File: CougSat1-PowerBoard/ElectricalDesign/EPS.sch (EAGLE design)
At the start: 250 parts, among them J1 PV0, J2 PV1, J3 PV2, J4 PV3, J5 Umbilical, J6 SWD, J7 CougSat Card, J8 Deployables, Q1 NTLUD3A50PZ, Q10 DMN2008LFU, Q11 DMN2008LFU, Q12 CSD25402Q3A, Q13 CSD25402Q3A, Q14 NTLUD3A50PZ, Q15 NTLUD3A50PZ, Q16 NTLUD3A50PZ, Q17 NTLUD3A50PZ, Q18 NTLUD3A50PZ, Q19 NTLUD3A50PZ, Q2 NTLUD3A50PZ, Q20 NTLUD3A50PZ, Q21 NTLUD3A50PZ, Q22 NTLUD3A50PZ, Q23 CSD25402Q3A, Q24 CSD25402Q3A, Q25 DMN53D0L, Q26 NTLUD3A50PZ, Q27 NTLUD3A50PZ, Q28 NTLUD3A50PZ, Q29 NTLUD3A50PZ, Q3 NTLUD3A50PZ, Q30 NTLUD3A50PZ, Q31 NTLUD3A50PZ, Q32 NTLUD3A50PZ, Q33 NTLUD3A50PZ, Q34 NTLUD3A50PZ, Q35 NTLUD3A50PZ, Q36 NTLUD3A50PZ, Q37 NTLUD3A50PZ, Q38 NTLUD3A50PZ, Q39 NTLUD3A50PZ, Q4 NTLUD3A50PZ, Q40 NTLUD3A50PZ, Q41 NTLUD3A50PZ, Q42 NTLUD3A50PZ, Q43 NTLUD3A50PZ, Q5 NTLUD3A50PZ, Q6 NTLUD3A50PZ, Q7 NTLUD3A50PZ, Q8 NTLUD3A50PZ, Q9 NTLUD3A50PZ, SW1 D2MQ-1-TL, U1 BQ29700, U10 LTC2499, U11 LTC2499, U12 LTC2499, U13 LTC2499, U14 MCP1501-18, U15 LTC2499, U2 BQ29700, U3 TPS64200, U4 TPS64200, U5 STM32L476RGT, U6 TCA9535R, U7 SN74LVC244AR, U8 TCA9535R, U9 LTC2499

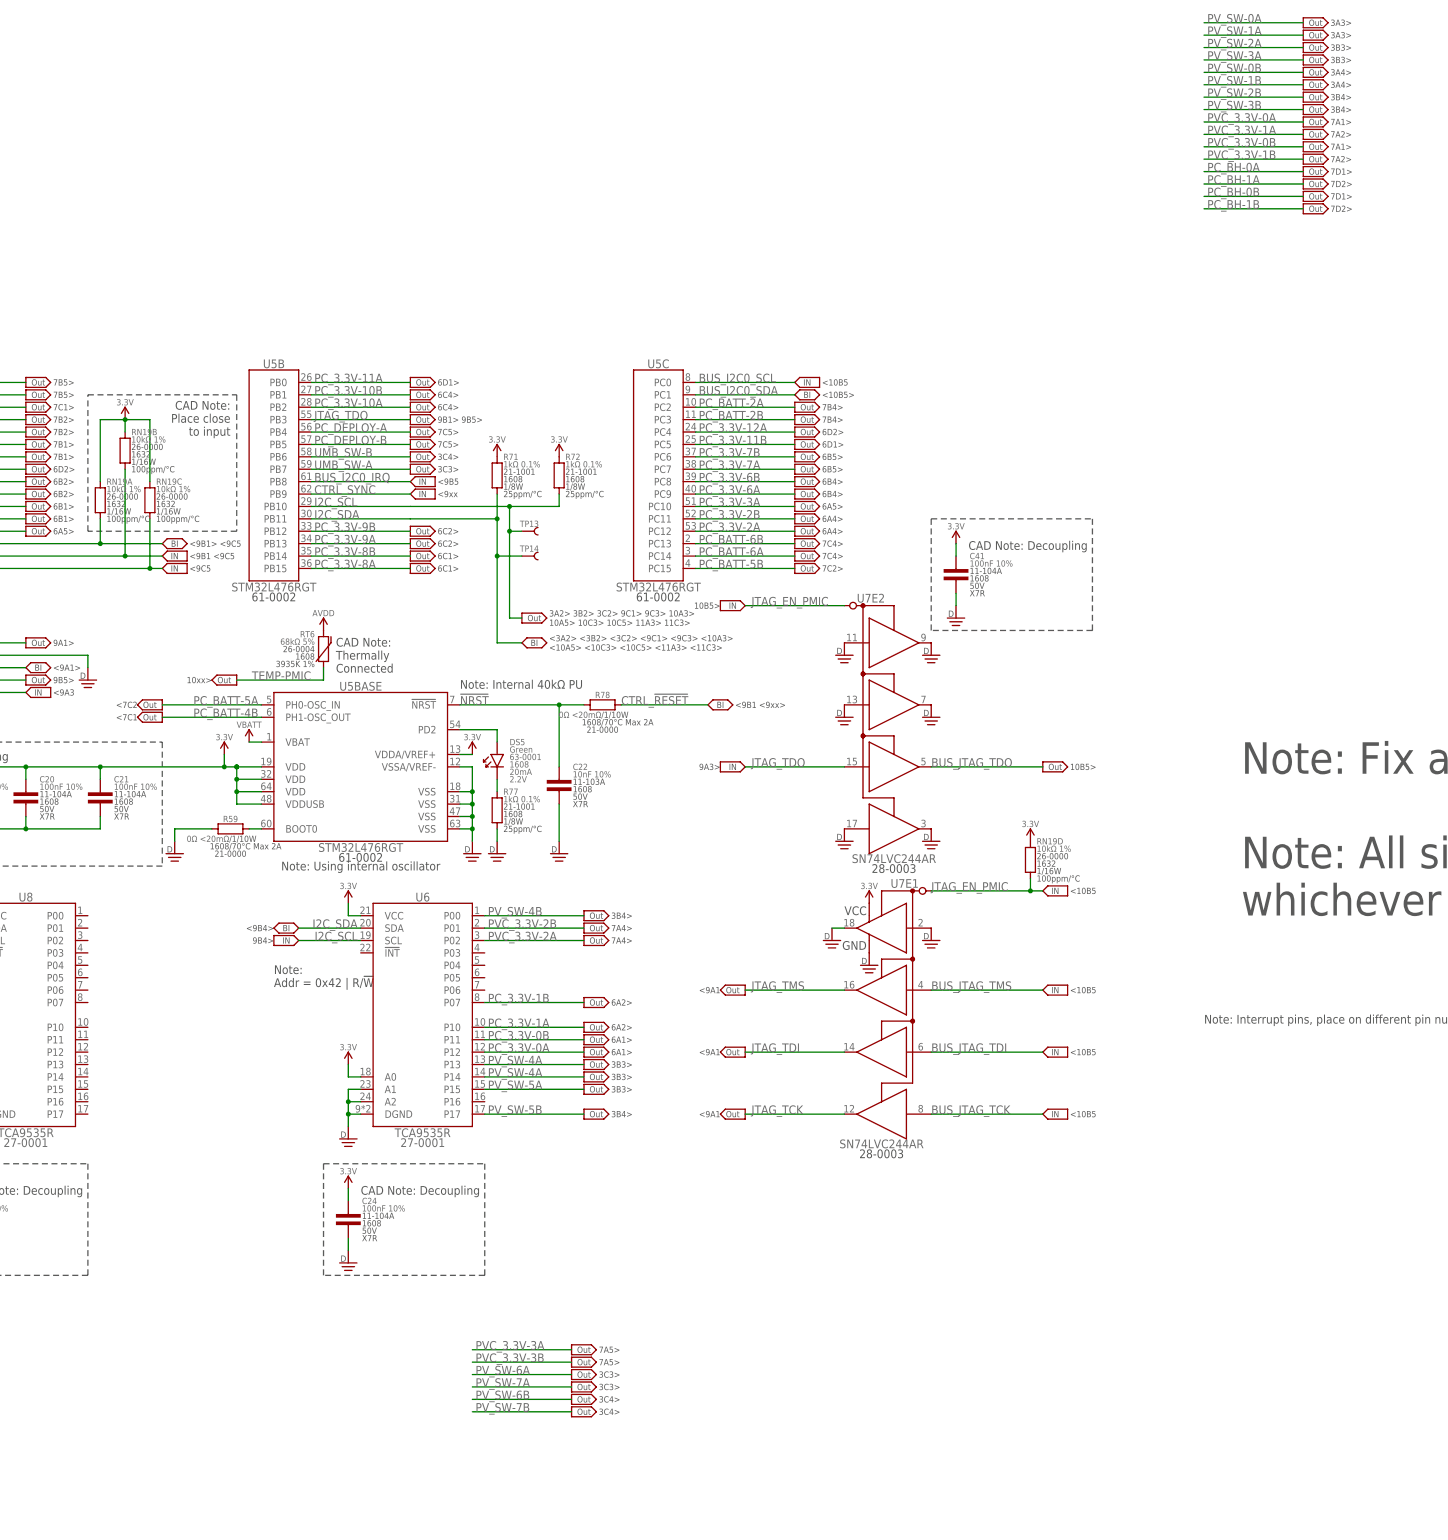
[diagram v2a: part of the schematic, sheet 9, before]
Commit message: Laid Out 3V3A Regulator
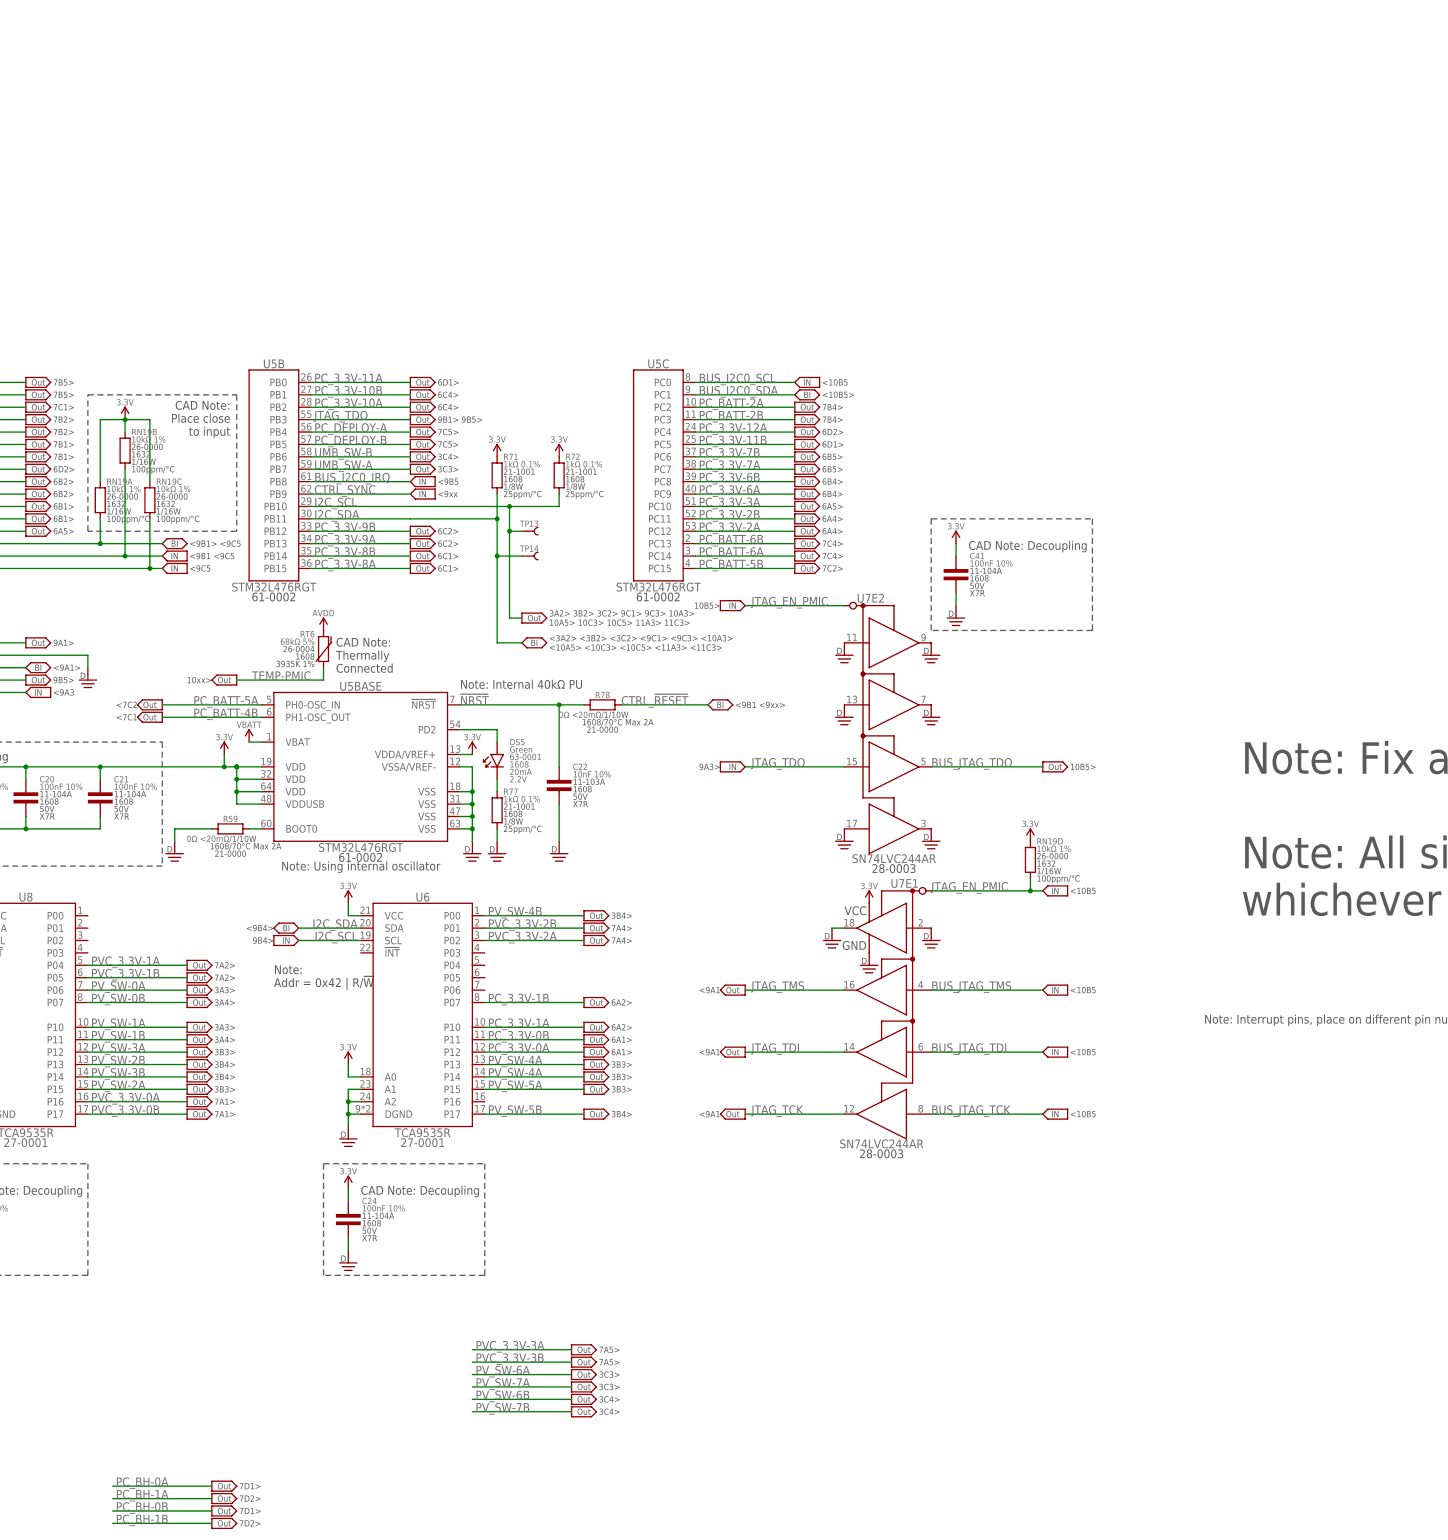
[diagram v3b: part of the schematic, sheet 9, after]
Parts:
- removed RN4, RN5: 10kΩ 5%, CougsInSpace-Resistors:RES_BUS-10-10K-3264
- added R86, R87, R88, R89: 10kΩ 0.1%, CougsInSpace-Resistors:RES-V-10K-1608
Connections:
- net 3.3V: now also R86.2, R87.2, R88.2, R89.2; no longer RN4.C, RN5.C
- net 3.3V-A: now also U12.CH6
- net 3.3V_I-A: now also U12.CH7
- net 3.3V_ISENS-A: now also U12.CH8
- net BP_VSS-A: now also U12.CH13
- net BP_VSS-B: now also U12.CH11
- net BP_VSS_I-A: now also U12.CH12
- net BP_VSS_I-B: now also U12.CH10
- net I_BH-0: now also U12.CH3
- net PR_BH-0: now also U12.CH2
- net PVC_3.3V-0A: now also R86.1, U8.P16
- net PVC_3.3V-0B: now also R87.1, U8.P17
- net PVC_3.3V-1A: now also R88.1, U8.P04
- net PVC_3.3V-1B: now also R89.1, U8.P05
- net PVI_3.3V-0: now also U12.CH1
- net PVI_3.3V-1: now also U12.CH15
- net PV_3.3V-0: now also U12.CH0
- net PV_3.3V-1: now also U12.CH14
- net PV_SW-0A: now also U8.P06
- net PV_SW-0B: now also RN20.8, U8.P07; no longer RN20.2
- net PV_SW-1A: now also RN20.2, U8.P10; no longer RN20.3
- net PV_SW-1B: now also RN20.7, U8.P11; no longer RN20.4
- net PV_SW-2A: now also U8.P15
- net PV_SW-2B: now also U8.P13
- net PV_SW-3A: now also RN20.3, U8.P12; no longer RN20.7
- net PV_SW-3B: now also RN20.4, U8.P14; no longer RN20.8
- net VBATT-A: now also U12.CH5, U12.CH9
- net VIN-A: now also U12.CH4

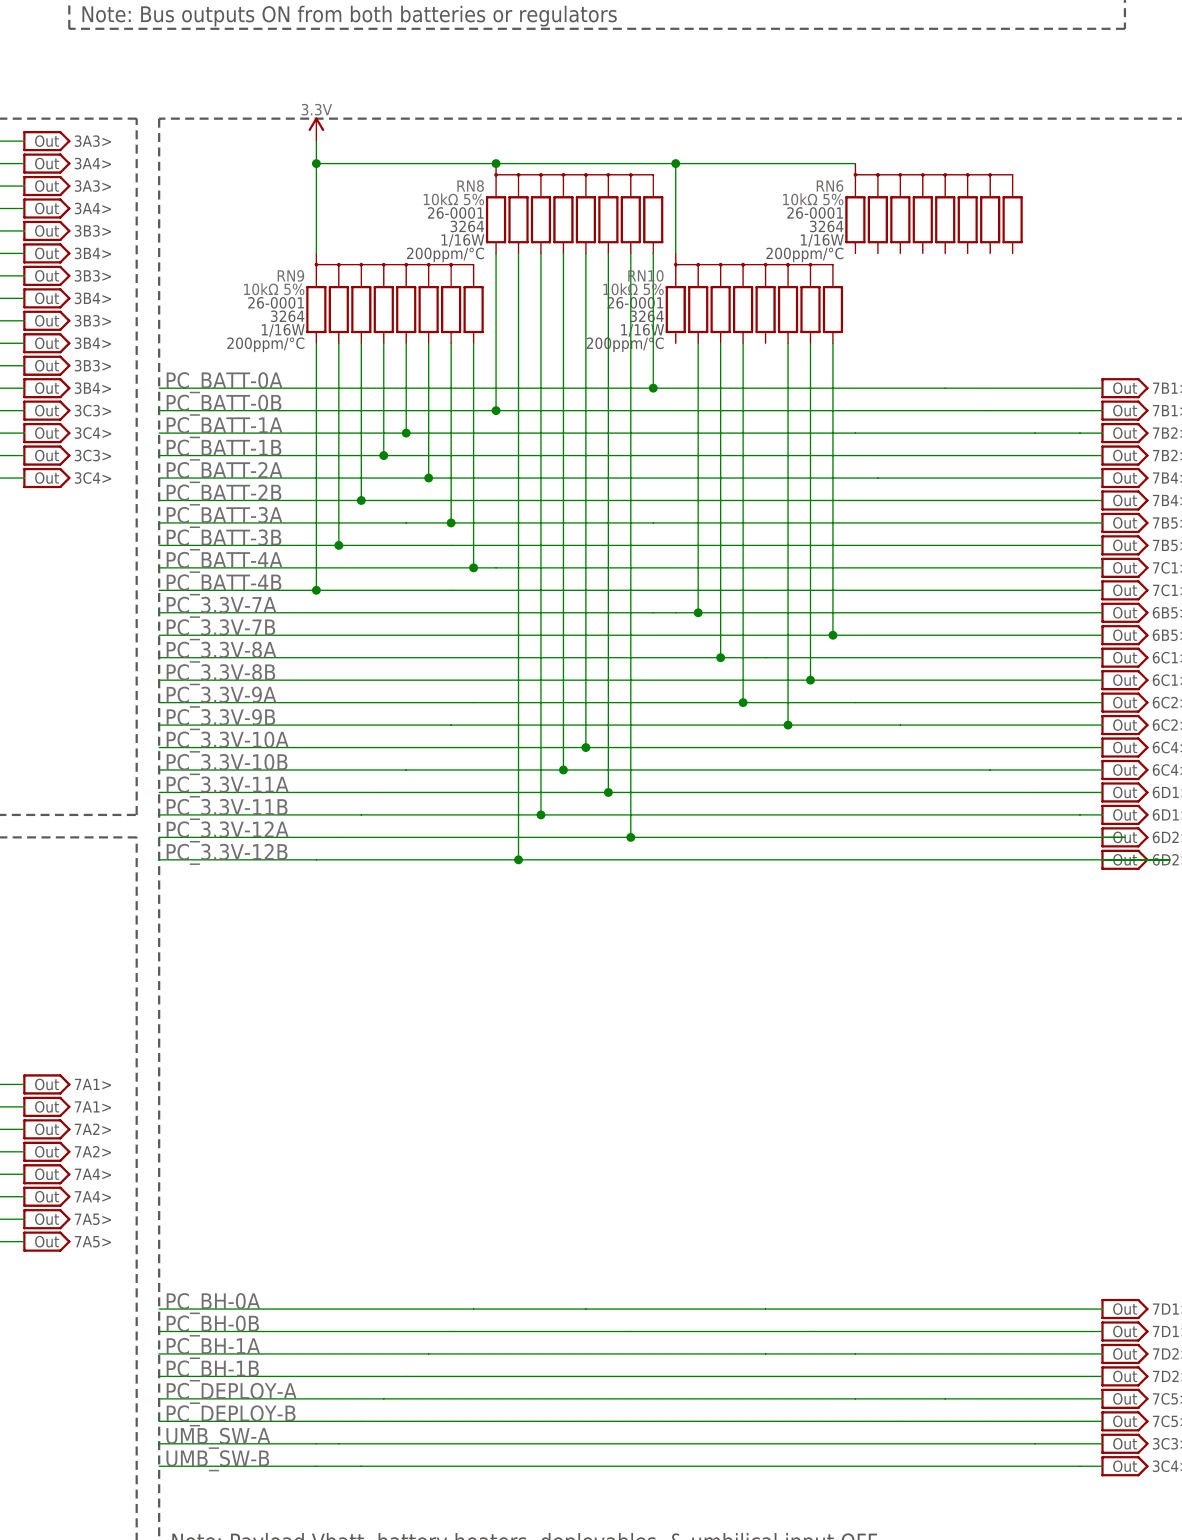
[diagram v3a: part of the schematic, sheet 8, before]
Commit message: Laid Out Voltage ADC
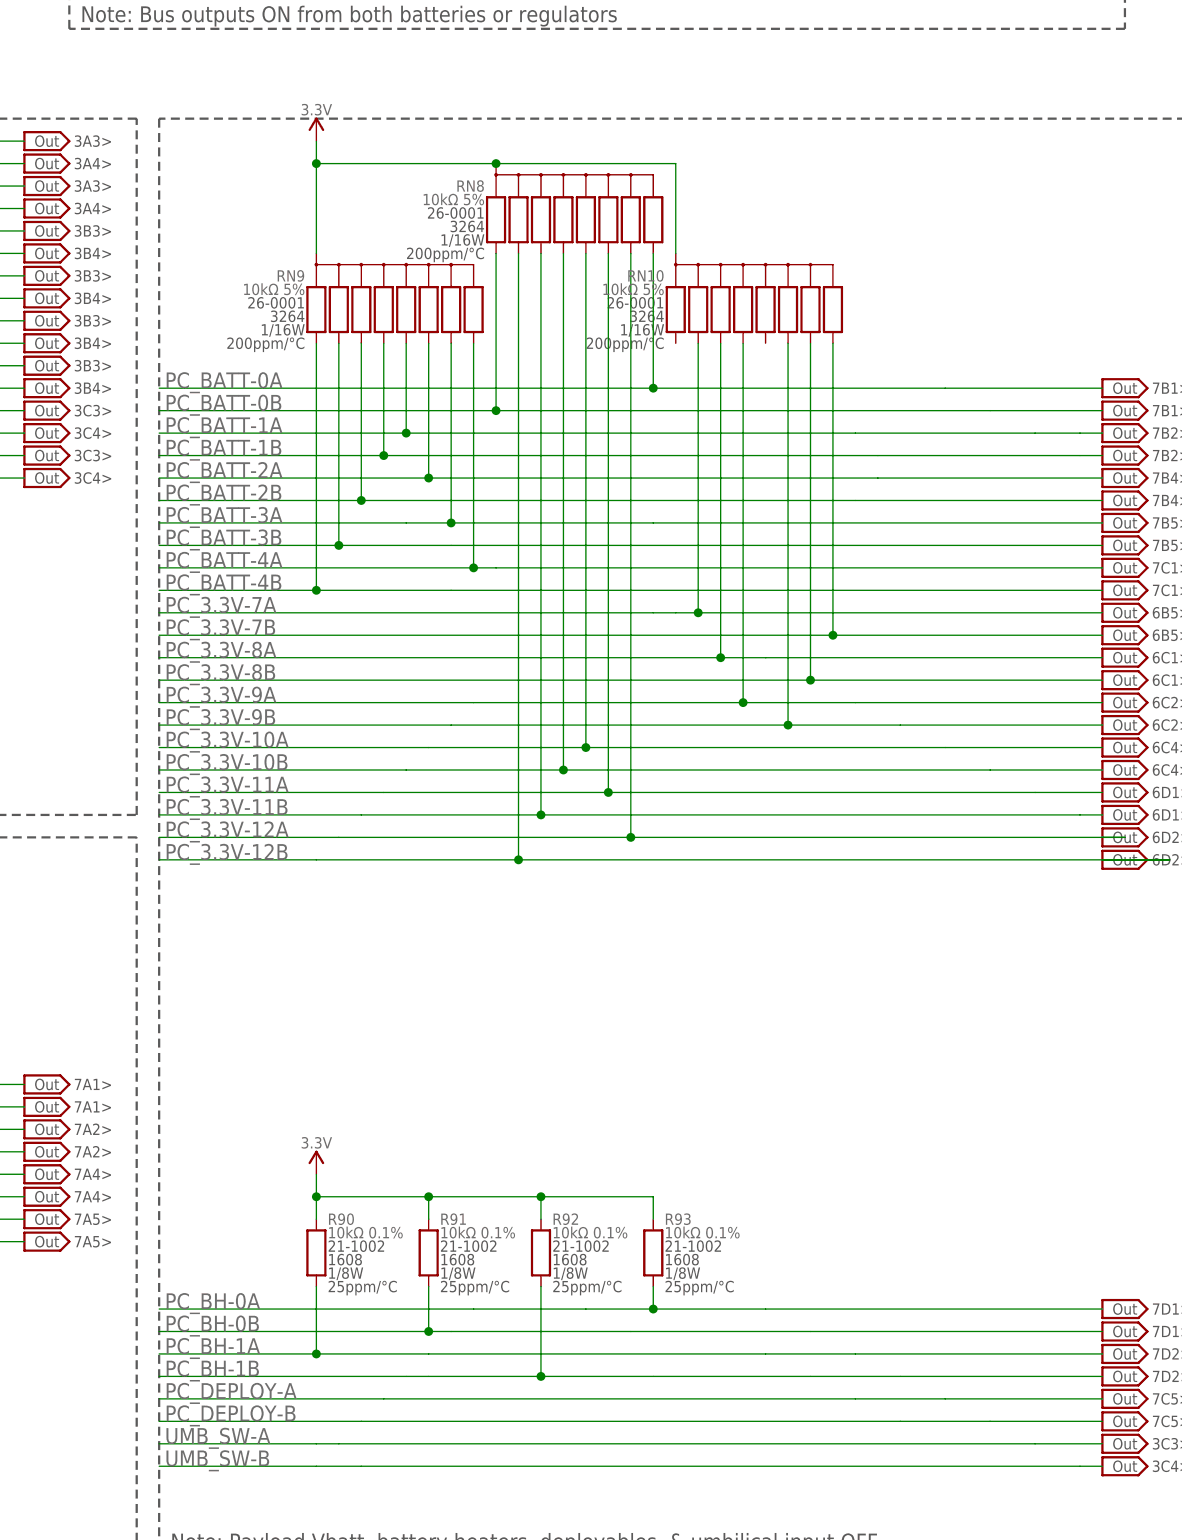
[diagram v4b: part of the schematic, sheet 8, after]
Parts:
- removed RN6: 10kΩ 5%, CougsInSpace-Resistors:RES_BUS-10-10K-3264
- added R90, R91, R92, R93: 10kΩ 0.1%, CougsInSpace-Resistors:RES-V-10K-1608
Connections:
- net 3.3V: now also R90.2, R91.2, R92.2, R93.2; no longer RN6.C
- net 3.3V-A: now also U13.CH11; no longer U13.CH13
- net 3.3V-B: now also U13.CH12; no longer U13.CH14
- net I_BH-0: now also U12.CH2; no longer U12.CH3
- net PC_BH-0A: now also R93.1, U8.P02
- net PC_BH-0B: now also R91.1, U8.P03
- net PC_BH-1A: now also R90.1, U8.P00
- net PC_BH-1B: now also R92.1, U8.P01
- net PR_BH-0: now also U12.CH3; no longer U12.CH2
- net TEMP+X+Y: now also U13.CH4; no longer U13.CH2
- net TEMP-BATT-B: now also U13.CH13; no longer U13.CH11
- net TEMP-PMIC: now also U13.CH2; no longer U13.CH4
- net TEMP-REG-B: now also U13.CH14; no longer U13.CH15
- net VBATT-B: now also U13.CH15; no longer U13.CH12

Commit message: Laid Out JTAG
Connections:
- net UMB_SW-A: now also U5B.PB6; no longer U5B.PB7
- net UMB_SW-B: now also U5B.PB7; no longer U5B.PB6
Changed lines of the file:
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@@
 <text x="154.94" y="-25.4" size="1.27" layer="97" align="center-left"> 3C4&gt;</text>
 <text x="76.2" y="58.42" size="1.27" layer="97" align="center-left"> 3A4&gt;</text>
-<text x="121.92" y="167.64" size="1.27" layer="97" align="center-left"> 3C3&gt;</text>
-<text x="121.92" y="170.18" size="1.27" layer="97" align="center-left"> 3C4&gt;</text>
+<text x="121.92" y="170.18" size="1.27" layer="97" align="center-left"> 3C3&gt;</text>
+<text x="121.92" y="167.64" size="1.27" layer="97" align="center-left"> 3C4&gt;</text>
 <text x="287.02" y="93.98" size="6.4516" layer="97" align="center-left">Note: Fix all off sheet designators linked to this sheet (JTAG too)
 Note: All signals above are GPIO, connect to any GPIO bank,
@@
 <net name="UMB_SW-A" class="0">
 <segment>
-<wire x1="96.52" y1="167.64" x2="116.84" y2="167.64" width="0.1524" layer="91"/>
-<label x="97.155" y="167.64" size="1.778" layer="95"/>
-<pinref part="U5" gate="B" pin="PB7"/>
-</segment>
-</net>
-<net name="UMB_SW-B" class="0">
-<segment>
 <wire x1="96.52" y1="170.18" x2="116.84" y2="170.18" width="0.1524" layer="91"/>
 <label x="97.155" y="170.18" size="1.778" layer="95"/>
@@
 </segment>
 </net>
+<net name="UMB_SW-B" class="0">
+<segment>
+<wire x1="96.52" y1="167.64" x2="116.84" y2="167.64" width="0.1524" layer="91"/>
+<label x="97.155" y="167.64" size="1.778" layer="95"/>
+<pinref part="U5" gate="B" pin="PB7"/>
+</segment>
+</net>
